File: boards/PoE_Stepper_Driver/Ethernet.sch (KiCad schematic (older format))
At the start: 64 parts, among them J1 RJ45_Shielded, Q1 NMOS_POE, U1 LT4321, U10 NMOS_POE, U11 NMOS_POE, U12 NMOS_POE, U13 NMOS_POE, U14 ICS1894, U2 LT4293, U6 NMOS_POE, U7 NMOS_POE, U8 NMOS_POE, U9 NMOS_POE

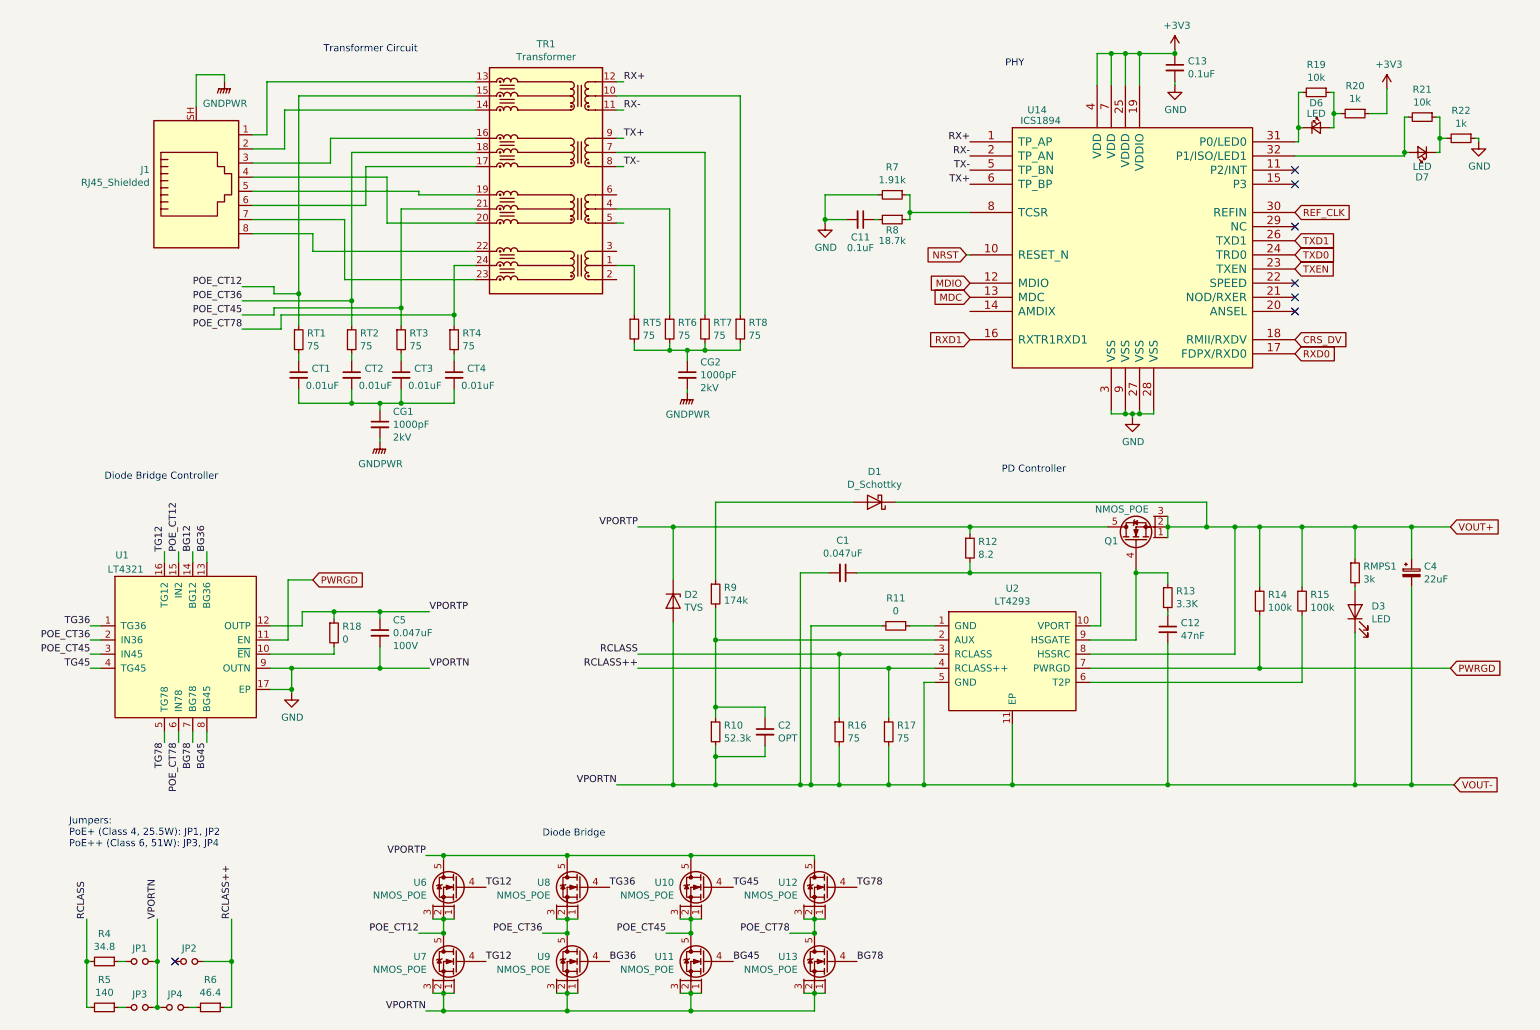
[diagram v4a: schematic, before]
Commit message: added dp83848 phy and more caps
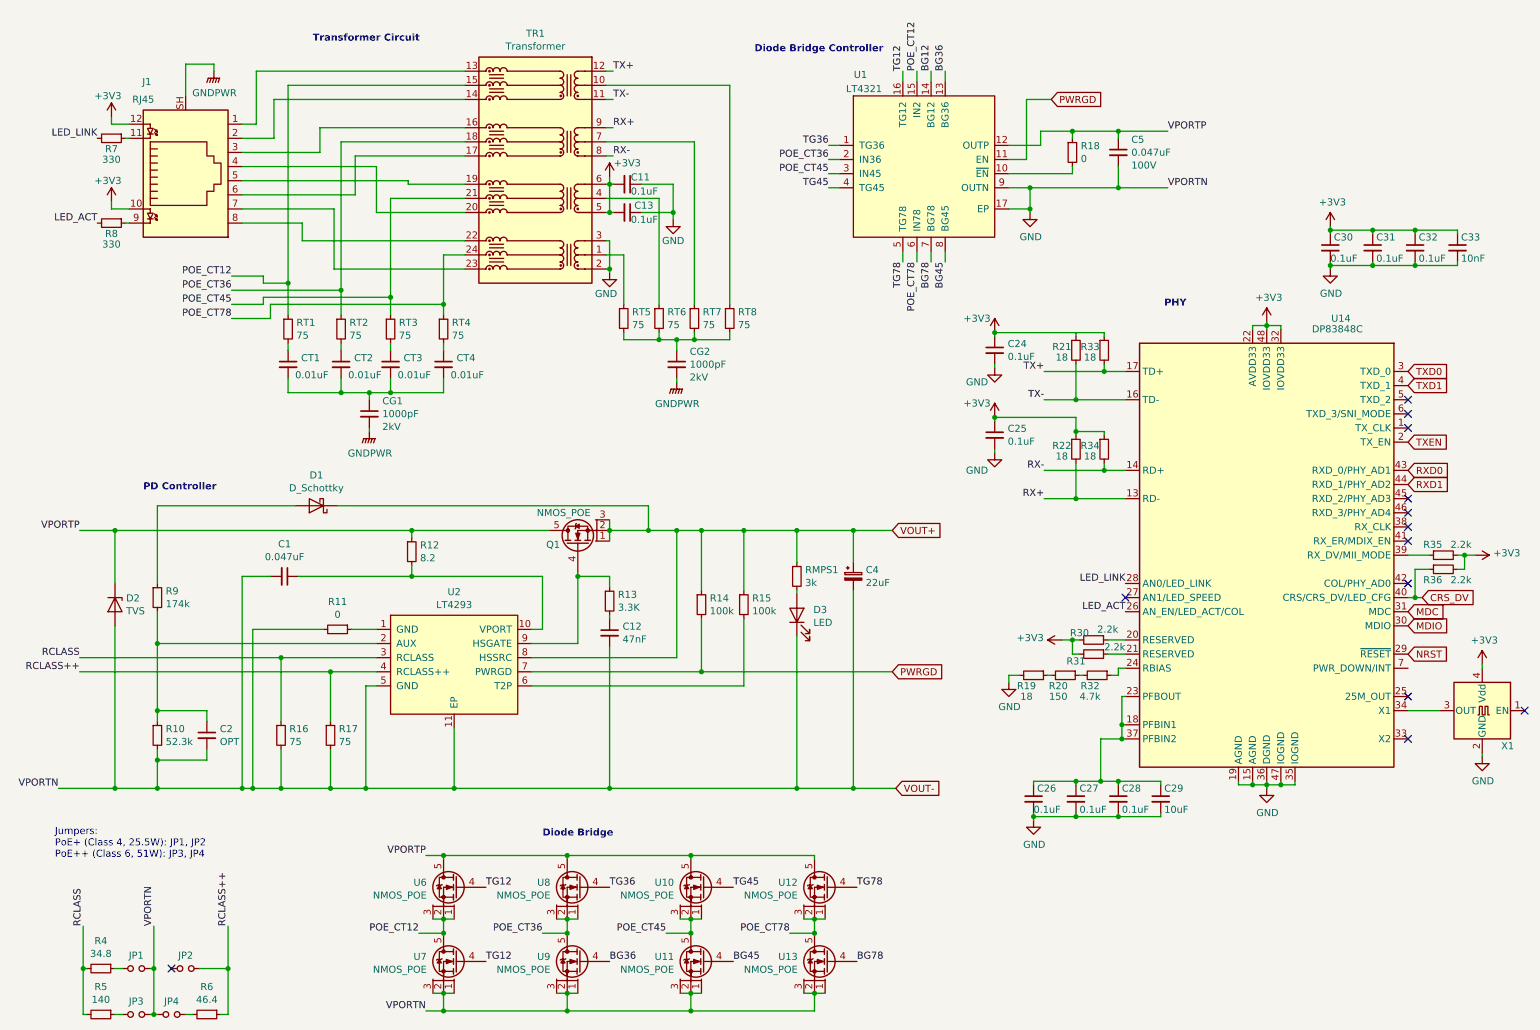
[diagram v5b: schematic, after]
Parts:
- removed D6, D7: LED, symbol device:LED_Small
- removed J1: RJ45_Shielded, symbol Connector:RJ45_Shielded
- removed U14: ICS1894, symbol ECE445:ICS1894
- added C24, C25, C26, C27, C28, C30, C31, C32: 0.1uF, symbol device:C_Small
- added C29: 10uF, symbol device:C_Small
- added C33: 10nF, symbol device:C_Small
- added J1: RJ45, symbol Connector:RJ45_LED_Shielded
- added R30, R31, R35, R36: 2.2k, symbol device:R_Small
- added R32: 4.7k, symbol device:R_Small
- added R33, R34: 18, symbol device:R_Small
- added U14: DP83848C, Package_QFP:LQFP-48_7x7mm_P0.5mm, symbol Interface_Ethernet:DP83848C
- added X1: TXC-7C, Oscillator:Oscillator_SMD_TXC_7C-4Pin_5.0x3.2mm, symbol Oscillator:TXC-7C
- R19, R21: value 10k -> 18
- R20: value 1k -> 150
- R22: value 1k -> 18
- R7: value 1.91k -> 330
- R8: value 18.7k -> 330
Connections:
- net +3V3: now also C11.2, C13.2, R21.1, R22.1, TR1.5 (TD2+), TR1.6 (TD2-), C24.1, C25.1, C30.1, C31.1, C32.1, C33.1, J1.10, J1.12, R30.2, R31.2, R33.1, R34.1, R35.2, R36.2, U14.22 (AVDD33), U14.32 (IOVDD33), U14.48 (IOVDD33), X1.4 (Vdd); no longer C13.1, R20.1
- net CRS_DV: now also R36.1, U14.40 (CRS/CRS_DV/LED_CFG)
- net GND: now also C11.1, C13.1, R19.2, TR1.2 (TD1+), TR1.3 (TD1-), C24.2, C25.2, C26.2, C27.2, C28.2, C29.2, C30.2, C31.2, C32.2, C33.2, U14.15 (AGND), U14.19 (AGND), U14.35 (IOGND), U14.36 (DGND), U14.47 (IOGND), X1.2 (GND); no longer C11.2, C13.2, R22.1, R7.2
- net GNDPWR: now also J1.SH
- net MDC: now also U14.31 (MDC)
- net MDIO: now also U14.30 (MDIO)
- net NRST: now also U14.29 (~RESET~)
- net RX+: now also R22.2, TR1.9 (TD3-), U14.13 (RD-); no longer TR1.12 (TD4-)
- net RX-: now also TR1.8 (TD3+), R34.2, U14.14 (RD+); no longer TR1.11 (TD4+)
- net RXD0: now also U14.43 (RXD_0/PHY_AD1)
- net RXD1: now also U14.44 (RXD_1/PHY_AD2)
- net TX+: now also TR1.12 (TD4-), R33.2, U14.17 (TD+); no longer TR1.9 (TD3-)
- net TX-: now also R21.2, TR1.11 (TD4+), U14.16 (TD-); no longer TR1.8 (TD3+)
- net TXD0: now also U14.3 (TXD_0)
- net TXD1: now also U14.4 (TXD_1)
- net TXEN: now also U14.2 (TX_EN)
- net at TR1.13 (MX4-): now also J1.1
- net at TR1.14 (MX4+): now also J1.2
- net at TR1.16 (MTX3-): now also J1.3
- net at TR1.17 (MTX3+): now also J1.6
- net at TR1.19 (MTX2-): now also J1.5
- net at TR1.20 (MTX2+): now also J1.4
- net at TR1.22 (MTX1-): now also J1.8
- net at TR1.23 (MTX1+): now also J1.7
- net at R7.1: now also J1.11; no longer R8.1
- net LED_ACT: now reaches R8.2
- net LED_ACT: now also U14.26 (AN_EN/LED_ACT/COL); no longer C11.1
- new net: C26.1, C27.1, C28.1, C29.1, U14.18 (PFBIN1), U14.23 (PFBOUT), U14.37 (PFBIN2)
- new net: R30.1, U14.20 (RESERVED)
- new net: R31.1, U14.21 (RESERVED)
- new net: R32.1, U14.24 (RBIAS)
- new net: U14.34 (X1), X1.3 (OUT)
- new net: R35.1, U14.39 (RX_DV/MII_MODE)
- new net: J1.9, R8.1
- new net: R20.1, R32.2
- new net LED_LINK: R7.2, U14.28 (AN0/LED_LINK)
- no-connect marks 7 -> 13
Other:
- moved on the sheet: C1, C12, C2, C4, C5, CG1, CG2, CT1, CT2, CT3, CT4, D1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

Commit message: started board layout
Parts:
- removed C2: OPT, symbol device:C_Small
- removed R16, R17: 75, symbol device:R_Small
- removed U10, U11, U12, U13, U6, U7, U8, U9: NMOS_POE, symbol ECE445:NMOS_POE
- added Q10, Q3, Q4, Q5, Q6, Q7, Q8, Q9: NMOS_POE, Package_SO:Vishay_PowerPAK_1212-8_Single, symbol ECE445:NMOS_POE
- C1, C5: footprint (none) -> Capacitor_SMD:C_0603_1608Metric_Pad1.05x0.95mm_HandSolder
- C26, C27, C28, C30, C31, C32, CT1, CT2, CT3, CT4: footprint (none) -> Capacitor_SMD:C_0805_2012Metric_Pad1.15x1.40mm_HandSolder
- C3: renamed from C12; footprint (none) -> Capacitor_SMD:C_0805_2012Metric_Pad1.15x1.40mm_HandSolder
- CG1, CG2: footprint (none) -> Capacitor_SMD:C_1812_4532Metric_Pad1.30x3.40mm_HandSolder
- D1, D2: footprint (none) -> Diode_SMD:D_SOD-128
- D3: footprint (none) -> LED_SMD:LED_0805_2012Metric_Pad1.15x1.40mm_HandSolder
- J1: footprint (none) -> Connector_RJ:RJ45_Amphenol_RJMG1BD3B8K1ANR
- Q1: footprint (none) -> Package_SO:Vishay_PowerPAK_1212-8_Single
- R10, R11, R13, R14, R15, R18, R19, R9, RT1, RT2, RT3, RT4, RT5, RT6, RT7, RT8: footprint (none) -> Resistor_SMD:R_0603_1608Metric_Pad1.05x0.95mm_HandSolder
- R12, R4, R5, R6, R7, R8: footprint (none) -> Resistor_SMD:R_0805_2012Metric_Pad1.15x1.40mm_HandSolder
- RMPS1: footprint (none) -> Resistor_SMD:R_2512_6332Metric_Pad1.52x3.35mm_HandSolder
- TR1: footprint Transformer_SMD:Transformer_Ethernet_HALO_TG111-MSC13 -> PoE_Stepper_Driver:PoE_Transformer
- U1: footprint (none) -> Package_DFN_QFN:QFN-16-1EP_4x4mm_P0.65mm_EP2.15x2.15mm
- U2: footprint (none) -> Package_SO:MSOP-10_3x3mm_P0.5mm
- X1: value TXC-7C -> SXO53C; footprint Oscillator:Oscillator_SMD_TXC_7C-4Pin_5.0x3.2mm -> PoE_Stepper_Driver:SXO53C
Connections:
- net BG12: now also Q8.4
- net BG36: now also Q6.4
- net BG45: now also Q4.4
- net BG78: now also Q10.4
- net GND: now also Q10.1, Q10.2, Q10.3, Q4.1, Q4.2, Q4.3, Q6.1, Q6.2, Q6.3, Q8.1, Q8.2, Q8.3
- net POE_CT12: now also Q7.1, Q7.2, Q7.3, Q8.5
- net POE_CT36: now also Q5.1, Q5.2, Q5.3, Q6.5
- net POE_CT45: now also Q3.1, Q3.2, Q3.3, Q4.5
- net POE_CT78: now also Q10.5, Q9.1, Q9.2, Q9.3
- net TG12: now also Q7.4
- net TG36: now also Q5.4
- net TG45: now also Q3.4
- net TG78: now also Q9.4
- net VPORTP: now also Q3.5, Q5.5, Q7.5, Q9.5
- no-connect marks 13 -> 14

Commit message: why tf is gnd connected to vout- bruhh
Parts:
- Q1, Q10, Q3, Q4, Q5, Q6, Q7, Q8, Q9: footprint Package_SO:Vishay_PowerPAK_1212-8_Single -> Package_TO_SOT_SMD:LFPAK33
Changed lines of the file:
@@
 F 0 "Q7" H 3594 6709 50  0000 L CNN
 F 1 "NMOS_POE" H 3594 6618 50  0000 L CNN
-F 2 "Package_SO:Vishay_PowerPAK_1212-8_Single" H 3405 7015 50  0001 C CNN
+F 2 "Package_TO_SOT_SMD:LFPAK33" H 3405 7015 50  0001 C CNN
 F 3 "" H 3405 7015 50  0001 C CNN
 	1    3475 6675
@@
 F 0 "Q5" H 4469 6709 50  0000 L CNN
 F 1 "NMOS_POE" H 4469 6618 50  0000 L CNN
-F 2 "Package_SO:Vishay_PowerPAK_1212-8_Single" H 4280 7015 50  0001 C CNN
+F 2 "Package_TO_SOT_SMD:LFPAK33" H 4280 7015 50  0001 C CNN
 F 3 "" H 4280 7015 50  0001 C CNN
 	1    4350 6675
@@
 F 0 "Q3" H 5344 6709 50  0000 L CNN
 F 1 "NMOS_POE" H 5344 6618 50  0000 L CNN
-F 2 "Package_SO:Vishay_PowerPAK_1212-8_Single" H 5155 7015 50  0001 C CNN
+F 2 "Package_TO_SOT_SMD:LFPAK33" H 5155 7015 50  0001 C CNN
 F 3 "" H 5155 7015 50  0001 C CNN
 	1    5225 6675
@@
 F 0 "Q9" H 6219 6709 50  0000 L CNN
 F 1 "NMOS_POE" H 6219 6618 50  0000 L CNN
-F 2 "Package_SO:Vishay_PowerPAK_1212-8_Single" H 6030 7015 50  0001 C CNN
+F 2 "Package_TO_SOT_SMD:LFPAK33" H 6030 7015 50  0001 C CNN
 F 3 "" H 6030 7015 50  0001 C CNN
 	1    6100 6675
@@
 F 0 "Q10" H 6219 7234 50  0000 L CNN
 F 1 "NMOS_POE" H 6219 7143 50  0000 L CNN
-F 2 "Package_SO:Vishay_PowerPAK_1212-8_Single" H 6030 7540 50  0001 C CNN
+F 2 "Package_TO_SOT_SMD:LFPAK33" H 6030 7540 50  0001 C CNN
 F 3 "" H 6030 7540 50  0001 C CNN
 	1    6100 7200
@@
 F 0 "Q4" H 5344 7234 50  0000 L CNN
 F 1 "NMOS_POE" H 5344 7143 50  0000 L CNN
-F 2 "Package_SO:Vishay_PowerPAK_1212-8_Single" H 5155 7540 50  0001 C CNN
+F 2 "Package_TO_SOT_SMD:LFPAK33" H 5155 7540 50  0001 C CNN
 F 3 "" H 5155 7540 50  0001 C CNN
 	1    5225 7200
@@
 F 0 "Q6" H 4469 7234 50  0000 L CNN
 F 1 "NMOS_POE" H 4469 7143 50  0000 L CNN
-F 2 "Package_SO:Vishay_PowerPAK_1212-8_Single" H 4280 7540 50  0001 C CNN
+F 2 "Package_TO_SOT_SMD:LFPAK33" H 4280 7540 50  0001 C CNN
 F 3 "" H 4280 7540 50  0001 C CNN
 	1    4350 7200
@@
 F 0 "Q8" H 3594 7234 50  0000 L CNN
 F 1 "NMOS_POE" H 3594 7143 50  0000 L CNN
-F 2 "Package_SO:Vishay_PowerPAK_1212-8_Single" H 3405 7540 50  0001 C CNN
+F 2 "Package_TO_SOT_SMD:LFPAK33" H 3405 7540 50  0001 C CNN
 F 3 "" H 3405 7540 50  0001 C CNN
 	1    3475 7200
@@
 F 0 "Q1" V 4325 4325 50  0000 C CNN
 F 1 "NMOS_POE" V 4550 4250 50  0000 C CNN
-F 2 "Package_SO:Vishay_PowerPAK_1212-8_Single" H 4355 4490 50  0001 C CNN
+F 2 "Package_TO_SOT_SMD:LFPAK33" H 4355 4490 50  0001 C CNN
 F 3 "" H 4355 4490 50  0001 C CNN
 	1    4425 4150

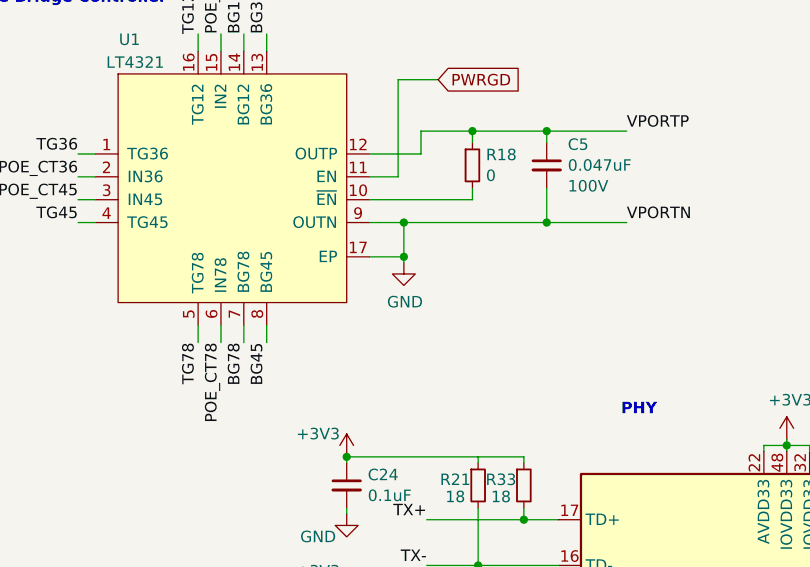
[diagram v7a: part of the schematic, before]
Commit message: fixed ground issue
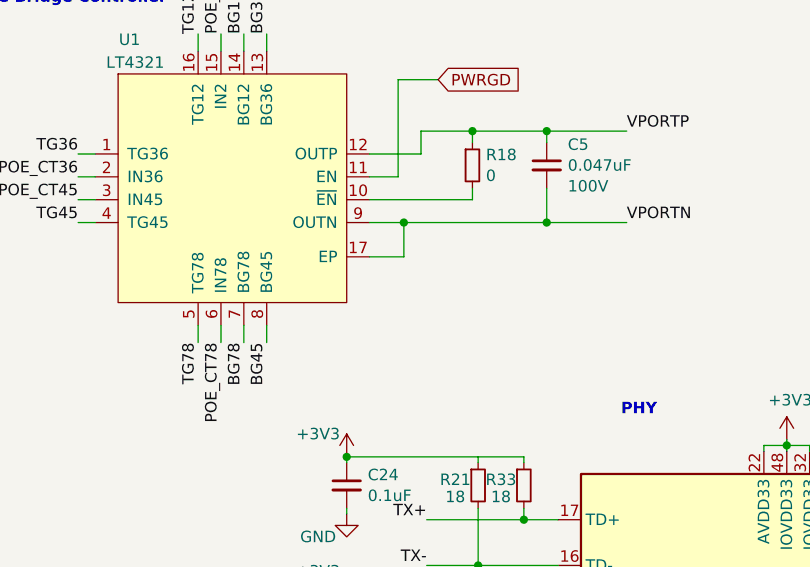
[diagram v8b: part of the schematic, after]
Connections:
- net GND: no longer C1.2, C3.2, C4.2, C5.2, D2.2 (A), D3.1 (K), JP1.2, JP3.2, JP4.1, Q10.1, Q10.2, Q10.3, Q4.1, Q4.2, Q4.3, Q6.1, Q6.2, Q6.3, Q8.1, Q8.2, Q8.3, R10.2, R11.2, U1.17 (EP), U1.9 (OUTN), U2.11 (EP), U2.5 (GND)
- new net VOUT-: C1.2, C3.2, C4.2, C5.2, D2.2 (A), D3.1 (K), JP1.2, JP3.2, JP4.1, Q10.1, Q10.2, Q10.3, Q4.1, Q4.2, Q4.3, Q6.1, Q6.2, Q6.3, Q8.1, Q8.2, Q8.3, R10.2, R11.2, U1.17 (EP), U1.9 (OUTN), U2.11 (EP), U2.5 (GND)
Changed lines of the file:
@@
 Wire Wire Line
 	7025 2250 7025 2175
-$Comp
-L power:GND #PWR04
-U 1 1 620EF51F
-P 7625 1900
-F 0 "#PWR04" H 7625 1650 50  0001 C CNN
-F 1 "GND" H 7630 1727 50  0000 C CNN
-F 2 "" H 7625 1900 50  0001 C CNN
-F 3 "" H 7625 1900 50  0001 C CNN
-	1    7625 1900
-	1    0    0    -1
-$EndComp
 Wire Wire Line
 	7475 1875 7625 1875
-Wire Wire Line
-	7625 1875 7625 1900
 Wire Wire Line
 	7625 1725 7625 1875
@@
 Wire Wire Line
 	7625 1725 8250 1725
-Connection ~ 7625 1875
 Text Label 8600 1325 0    50   ~ 0
 VPORTP
